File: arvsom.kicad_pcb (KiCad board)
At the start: 12 copper layers, 55 x 40 mm, 407 parts, among them J1 TAG-10PIN, J3 DF40C-100DP-0.4V(51), J4 DF40C-100DP-0.4V(51), Q1 DMG1013UWQ-7, Q5 DMG1012UW, U1 MT53D1024M32D4DT-053, U10 TDA19988BHN_C1,557, U11 KSZ9031RNXCA, U13 VIC7100, U2 GD25LQ256DWIGR, U3 MT53D1024M32D4DT-053, U4 CSD86330Q3D, U5 LMR62014XMF_NOPB, U6 CSD86330Q3D, U7 STM811RW16F, U8 TPS65086100, Y1 ABM8G-25.000MHZ-18-D2Y-T, Y2 ABM8G-25.000MHZ-18-D2Y-T, Y3 ABM8G-27.000MHZ-18-D2Y-T

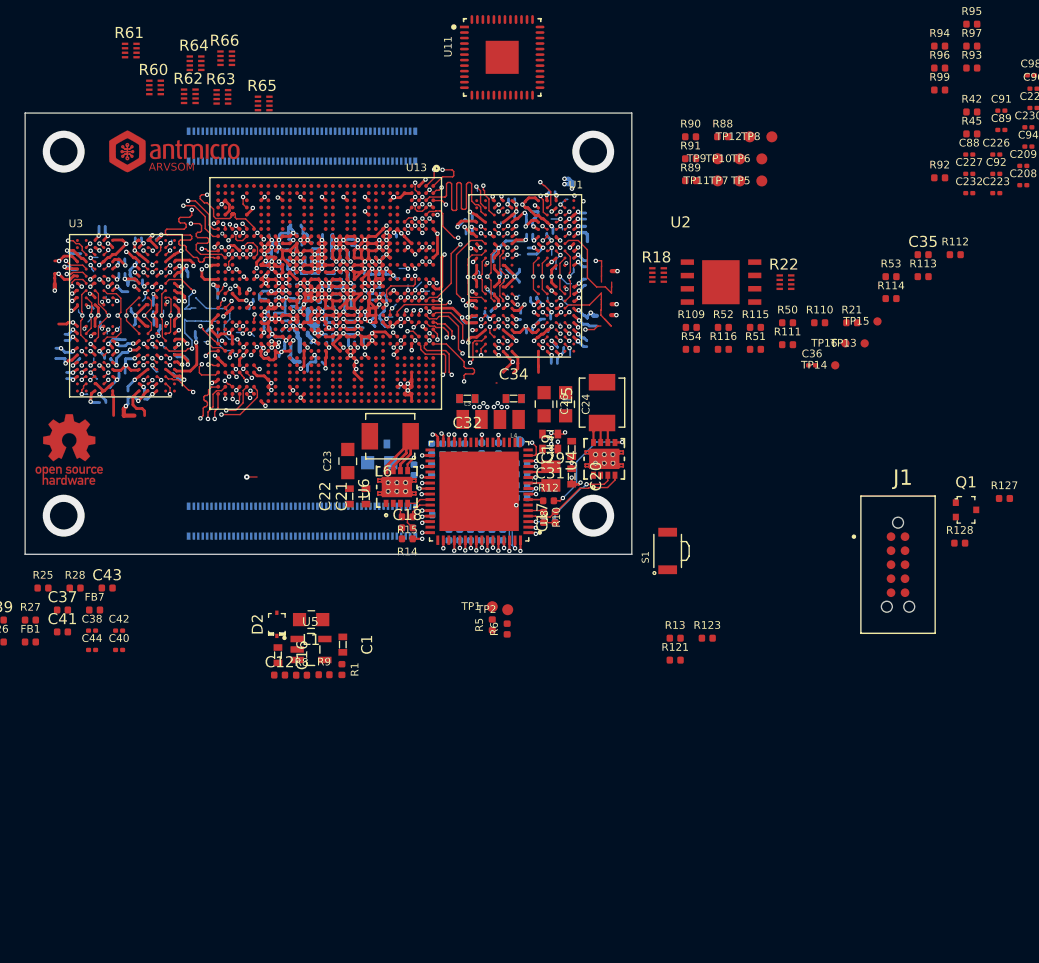
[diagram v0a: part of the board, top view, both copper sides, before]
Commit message: Changed VIC pad size
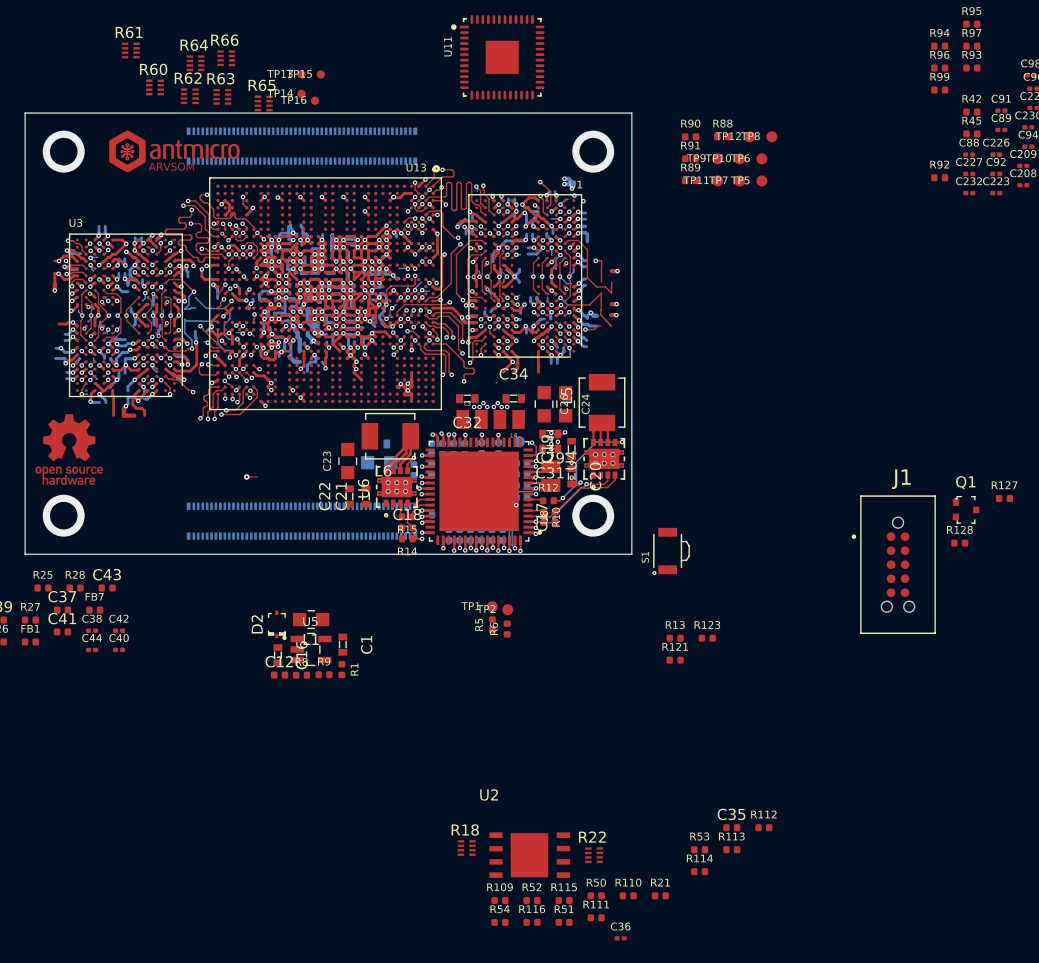
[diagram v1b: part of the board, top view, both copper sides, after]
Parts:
- moved TP13 56.6 mm to (155.1, 51.5)
- moved TP15 55.2 mm to (156.8, 51.5)
- moved R110 54.8 mm to (184.7, 125.9)
- moved R53 54.8 mm to (191.2, 121.8)
- moved C35 54.8 mm to (194.1, 119.8)
- moved C36 54.8 mm to (184.0, 129.8)
- moved R111 54.8 mm to (181.8, 127.9)
- moved R112 54.8 mm to (197.0, 119.8)
- moved R113 54.8 mm to (194.1, 121.8)
- moved R114 54.8 mm to (191.2, 123.7)
- moved R116 54.8 mm to (176.0, 128.3)
- moved R21 54.8 mm to (187.6, 125.9)
- moved R22 54.8 mm to (181.6, 122.2)
- moved R50 54.8 mm to (181.8, 125.9)
- moved R51 54.8 mm to (178.9, 128.3)
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
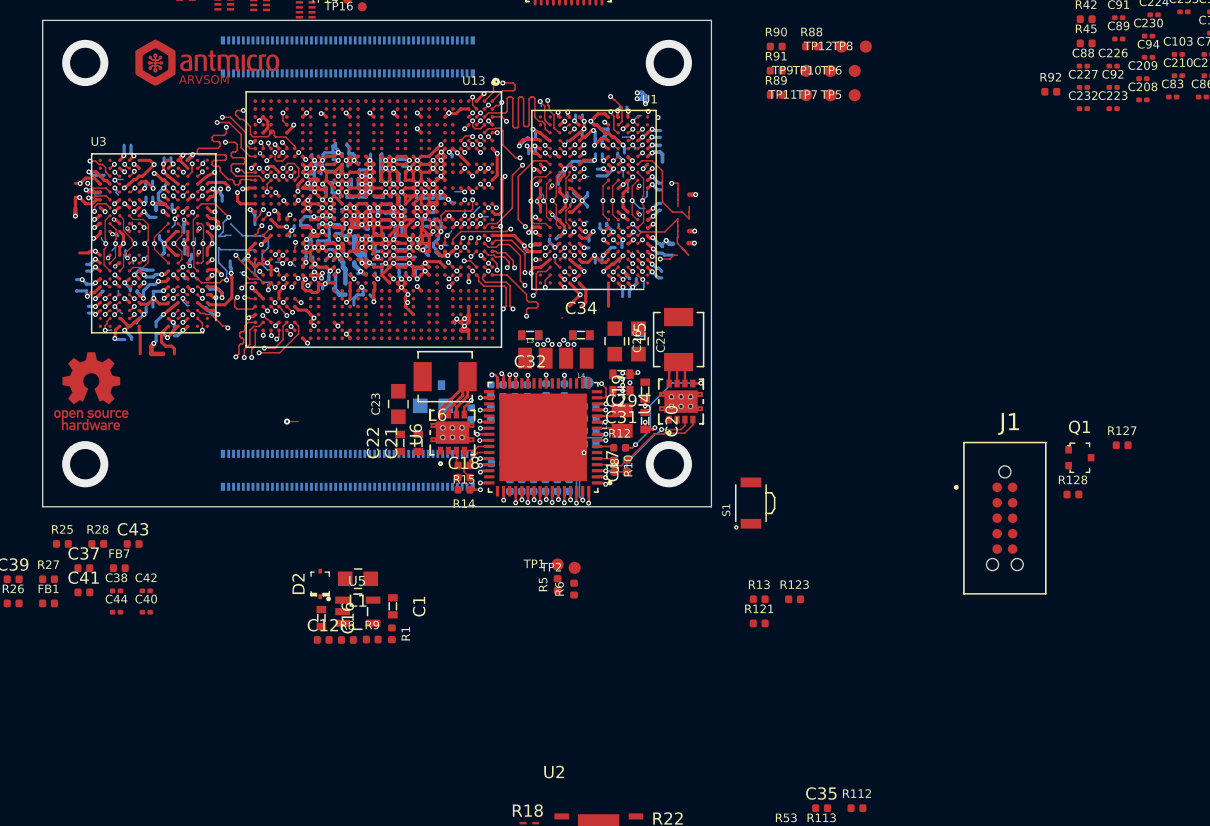
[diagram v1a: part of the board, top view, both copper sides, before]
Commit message: Fixed DRC errors in DDR area
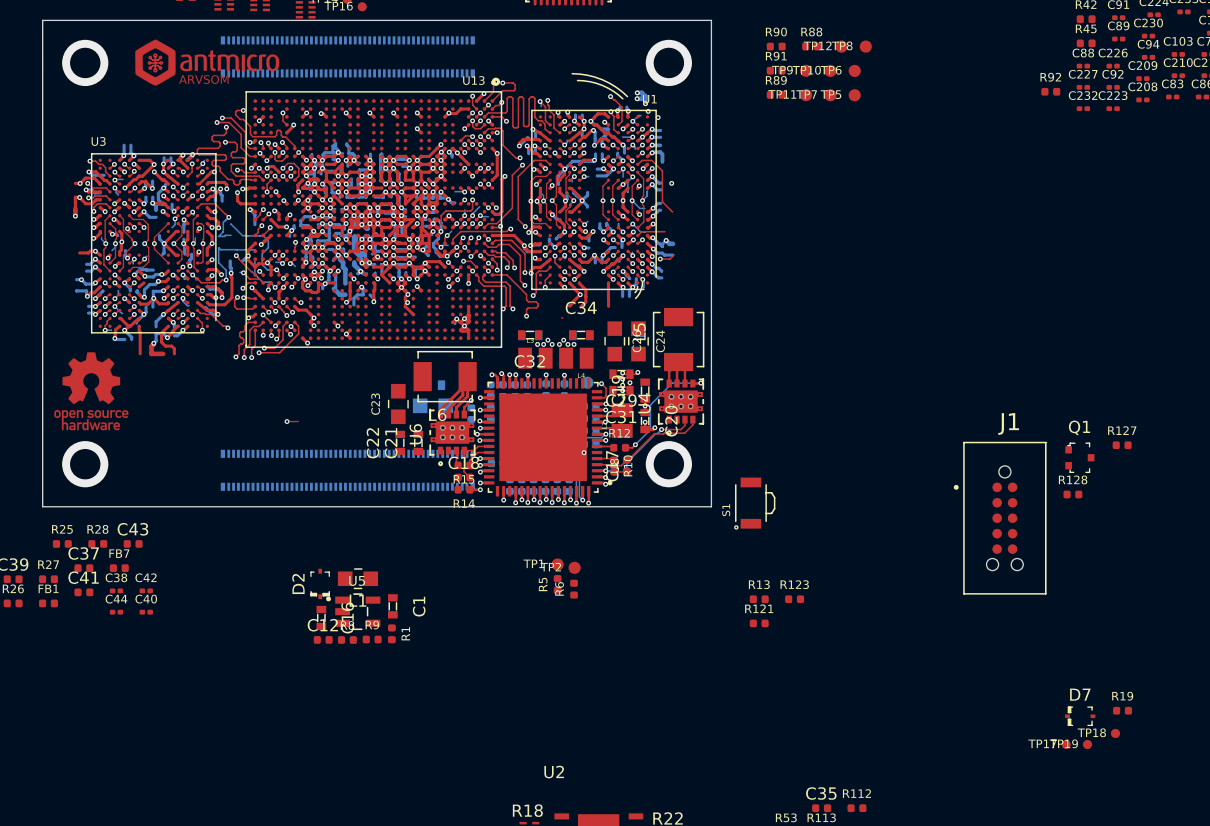
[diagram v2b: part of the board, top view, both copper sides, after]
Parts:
- added D7: PMEG3010CEJ, arvsom-footprints:SOD-323F, F.Cu at (215.3, 112.2)
- added R19: R_1k_0402, arvsom-footprints:0402-res, F.Cu at (218.8, 111.7)
- added TP17: TP_SMD_0_75MM, arvsom-footprints:Testpoint_smd_0_75mm, F.Cu at (214.2, 114.6)
- added TP18: TP_SMD_0_75MM, arvsom-footprints:Testpoint_smd_0_75mm, F.Cu at (218.2, 113.7)
- added TP19: TP_SMD_0_75MM, arvsom-footprints:Testpoint_smd_0_75mm, F.Cu at (215.9, 114.6)
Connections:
- TP13 pad 1: Net-(TP13-Pad1) -> /VIC7100 config/ATEMP_TEST0
- TP14 pad 1: Net-(TP14-Pad1) -> /VIC7100 config/ATEMP_TEST1
- TP15 pad 1: Net-(TP15-Pad1) -> /VIC7100 config/ATEMP_VSS
- TP16 pad 1: Net-(TP16-Pad1) -> /VIC7100 config/ATEMP_VCAL
- U1 pad G2: DDR0_ODT_0 -> DDR0_ODT0
- U1 pad T2: DDR0_ODT_1 -> DDR0_ODT1
- U13 pad AK16: DDR1_CK1_P -> DDR1_CK1_N
- U13 pad AL16: DDR1_CK1_N -> DDR1_CK1_P
- U3 pad G2: DDR1_ODT_0 -> DDR1_ODT0
- U3 pad R3: DDR_CS3 -> DDR1_CS3
- U3 pad T2: DDR1_ODT_1 -> DDR1_ODT1
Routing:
- net DDR0_ODT1: track 13.8 -> 29.2 mm
- net DDR0_ODT_1: track 8.84 -> 0.00 mm
- net DDR1_ODT_0: track 8.61 -> 0.00 mm, vias 1 -> 0
- net DDR1_ODT0: track 3.70 -> 12.3 mm, vias 1 -> 2
- net DDR0_ODT_0: track 8.09 -> 0.00 mm
- net DDR1_DQ08: track 18.9 -> 26.4 mm
- net GND: track 417.9 -> 411.2 mm, vias 241 -> 239
- net DDR1_ODT_1: track 6.15 -> 0.00 mm, vias 1 -> 0
- net DDR1_ODT1: track 7.69 -> 13.8 mm, vias 1 -> 2
- net DDR1_DQ10: track 19.2 -> 24.7 mm
- net DDR0_DQ17: track 18.5 -> 23.5 mm
- net DDR1_DQ25: track 14.3 -> 19.3 mm
- net DDR0_DMI2: track 18.5 -> 22.8 mm
- net DDR0_ODT0: track 19.5 -> 21.6 mm
- net DDR0_DQ00: track 21.6 -> 23.1 mm
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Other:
- rule trace_min: 0.127 -> 0.0762

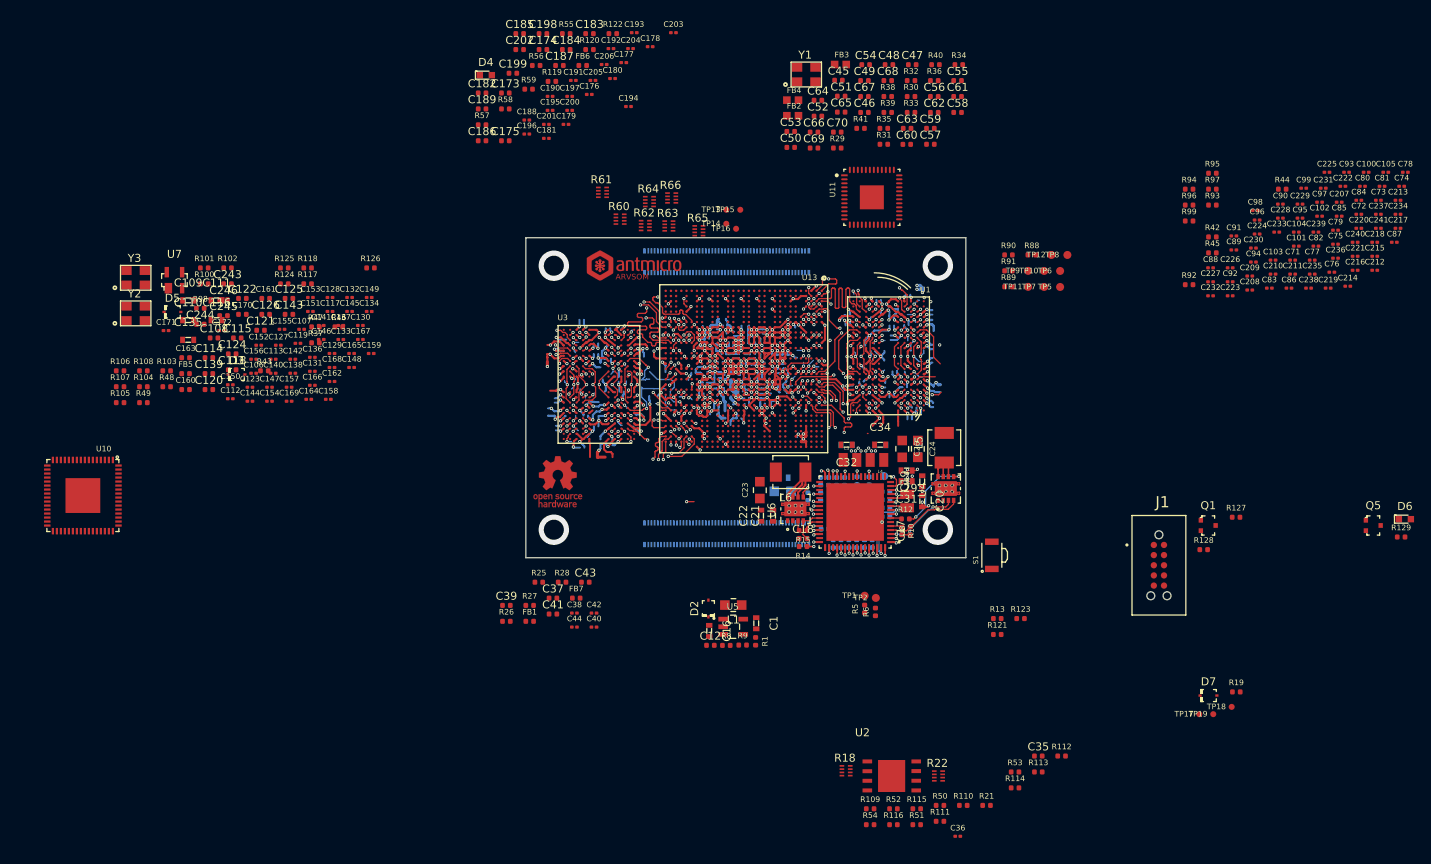
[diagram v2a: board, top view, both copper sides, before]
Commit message: Grouping components for framer placement
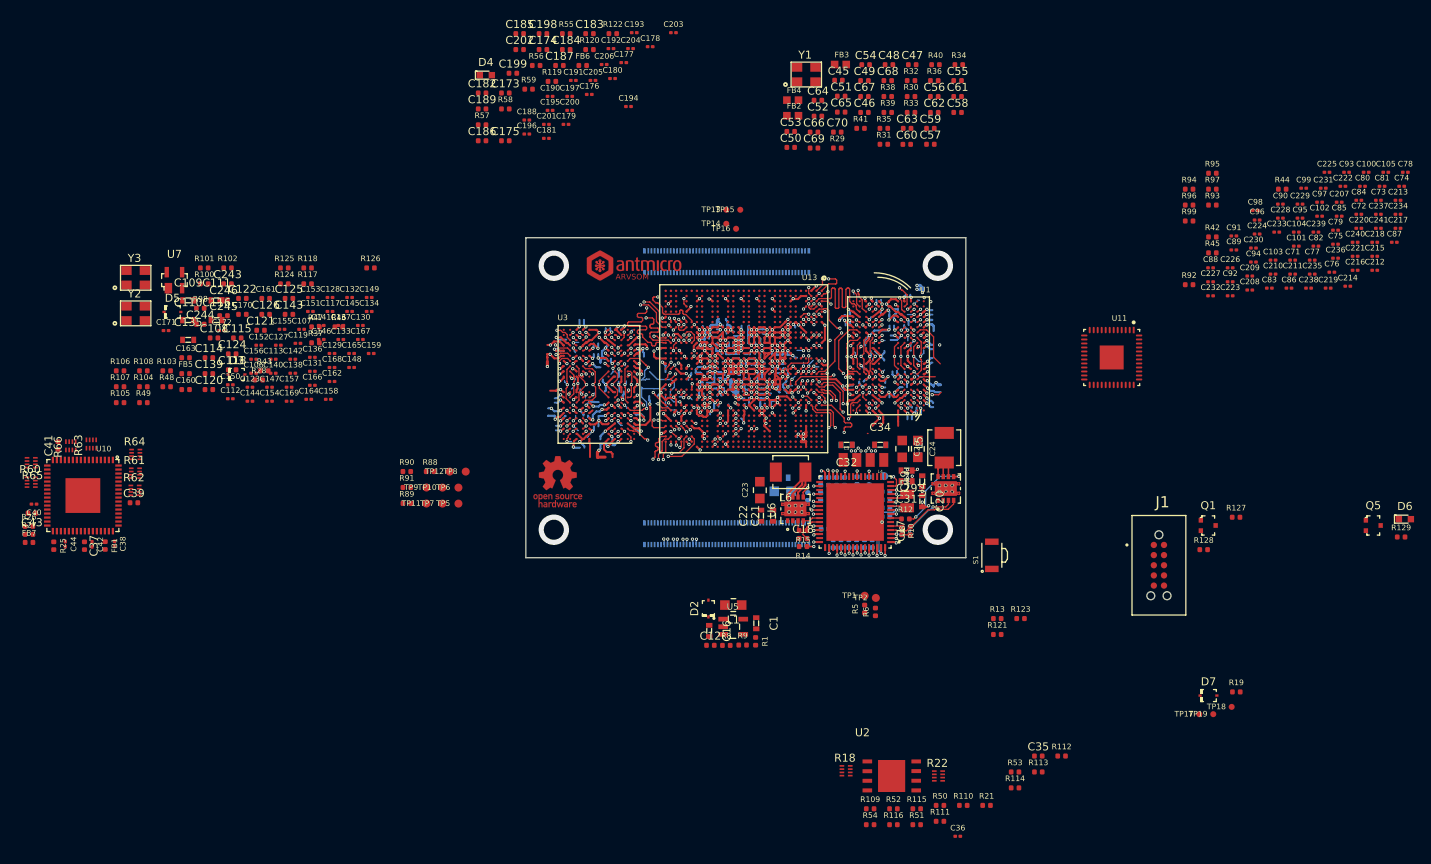
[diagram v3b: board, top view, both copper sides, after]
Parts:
- moved R65 88.4 mm to (68.2, 83.1), turned to 180 degrees
- moved R66 81.2 mm to (73.1, 81.0), turned to 90 degrees
- moved R60 80.6 mm to (68.2, 85.5)
- moved R88 79.9 mm to (118.0, 84.2)
- moved R89 79.9 mm to (115.1, 88.2)
- moved R90 79.9 mm to (115.1, 84.2)
- moved TP10 79.9 mm to (119.6, 86.3)
- moved TP11 79.9 mm to (117.6, 88.2)
- moved TP12 79.9 mm to (120.5, 84.3)
- moved TP5 79.9 mm to (121.6, 88.3)
- moved TP6 79.9 mm to (121.6, 86.3)
- moved TP7 79.9 mm to (119.6, 88.3)
- moved TP8 79.9 mm to (122.5, 84.3)
- moved TP9 79.9 mm to (117.6, 86.2)
- moved R91 79.9 mm to (115.1, 86.2)
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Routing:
- net HDMI_TXC_N: track 0.00 -> 23.5 mm, vias 0 -> 1
- net HDMI_TXC_P: track 0.00 -> 23.5 mm, vias 0 -> 1
- net HDMI_TX0_N: track 0.00 -> 23.3 mm, vias 0 -> 1
- net HDMI_TX0_P: track 0.00 -> 23.3 mm, vias 0 -> 1
- net HDMI_TX1_N: track 0.00 -> 23.3 mm, vias 0 -> 1
- net HDMI_TX1_P: track 0.00 -> 23.3 mm, vias 0 -> 1
- net HDMI_TX2_P: track 0.00 -> 23.0 mm, vias 0 -> 1
- net HDMI_TX2_N: track 0.00 -> 22.8 mm, vias 0 -> 1
- net AVDD3V3_USB: track 3.21 -> 1.03 mm
- net VCC_3V3: track 34.0 -> 31.9 mm
- net /VIC7100 config/ATEMP_VSS: track 2.54 -> 0.60 mm
- net GND: track 411.2 -> 410.0 mm
- net LCD_DATA3: track 0.94 -> 0.00 mm, vias 1 -> 0
- net RGMII_RXD1: track 0.00 -> 0.46 mm, vias 0 -> 1
- net RGMII_TXD2: track 0.00 -> 0.46 mm, vias 0 -> 1
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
